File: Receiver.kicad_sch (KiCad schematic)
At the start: 45 parts, among them J2 UFL, J3 UFL, SW2 TS2306A, U1 ESP32-C3, U11 TPRT9013-33, U12 0479480001, U9 SX1280IMLTRT, Y1 40MHz, Y2 52MHz/10ppm

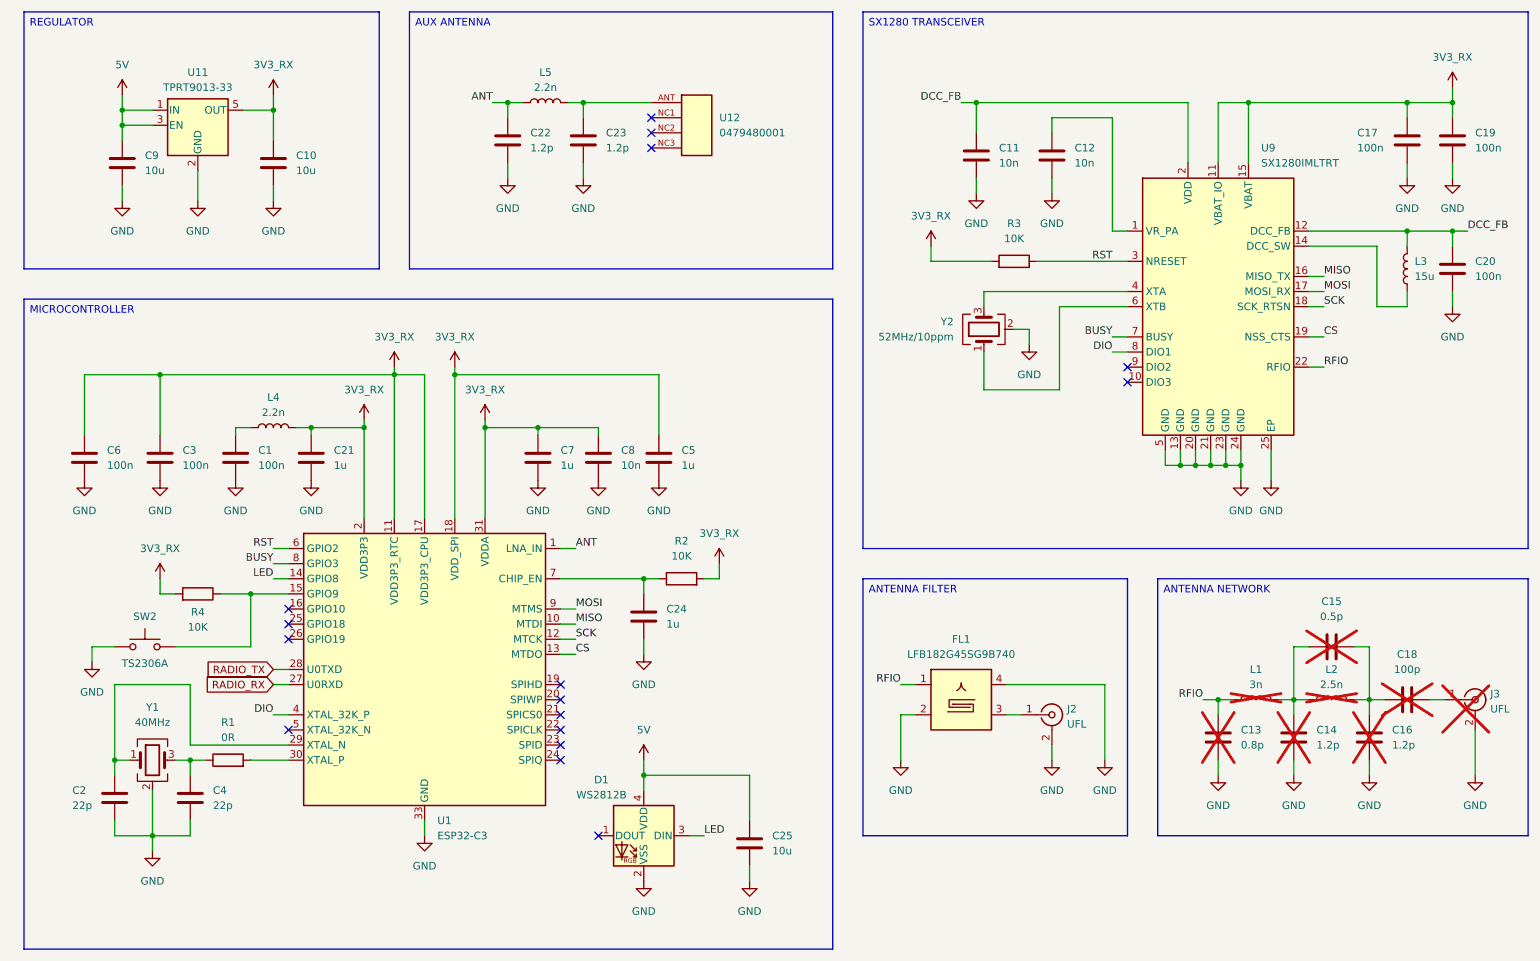
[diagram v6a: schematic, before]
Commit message: Footprints and revision
Added the missing footprints.
Updated a all the schematics.
Completed an initial review of the schematics.

TODO:
Perform a deep review of the schematics before committing to layout.
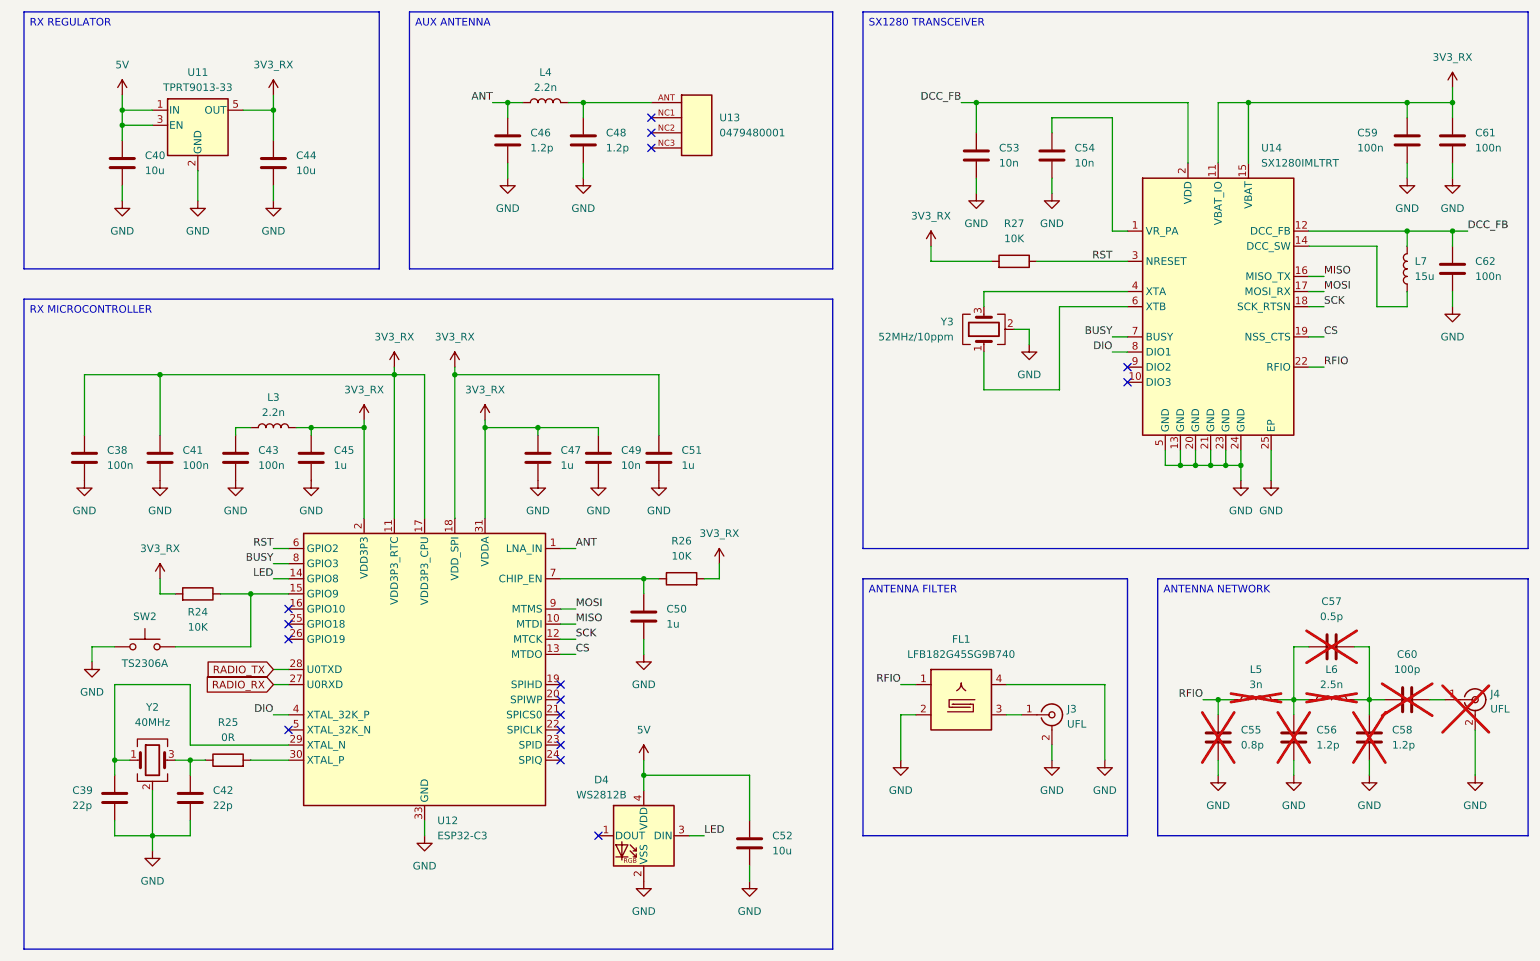
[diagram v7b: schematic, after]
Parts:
- C38: renamed from C6; footprint (none) -> Capacitor_SMD:C_0201_0603Metric
- C39: renamed from C2; footprint (none) -> Capacitor_SMD:C_0201_0603Metric
- C40: renamed from C9; footprint (none) -> Capacitor_SMD:C_0805_2012Metric
- C41: renamed from C3; footprint (none) -> Capacitor_SMD:C_0603_1608Metric
- C42: renamed from C4; footprint (none) -> Capacitor_SMD:C_0603_1608Metric
- C43: renamed from C1; footprint (none) -> Capacitor_SMD:C_0603_1608Metric
- C44: renamed from C10; footprint (none) -> Capacitor_SMD:C_0805_2012Metric
- C45: renamed from C21; footprint (none) -> Capacitor_SMD:C_0603_1608Metric
- C46: renamed from C22; footprint (none) -> Capacitor_SMD:C_0603_1608Metric
- C47: renamed from C7; footprint (none) -> Capacitor_SMD:C_0603_1608Metric
- C48: renamed from C23; footprint (none) -> Capacitor_SMD:C_0603_1608Metric
- C49: renamed from C8; footprint (none) -> Capacitor_SMD:C_0603_1608Metric
- C50: renamed from C24; footprint (none) -> Capacitor_SMD:C_0603_1608Metric
- C51: renamed from C5; footprint (none) -> Capacitor_SMD:C_0603_1608Metric
- C52: renamed from C25; footprint (none) -> Capacitor_SMD:C_0805_2012Metric
- C53: renamed from C11; footprint (none) -> Capacitor_SMD:C_0603_1608Metric
- C54: renamed from C12; footprint (none) -> Capacitor_SMD:C_0603_1608Metric
- C59: renamed from C17; footprint (none) -> Capacitor_SMD:C_0603_1608Metric
- C61: renamed from C19; footprint (none) -> Capacitor_SMD:C_0603_1608Metric
- C62: renamed from C20; footprint (none) -> Capacitor_SMD:C_0603_1608Metric
- L3: renamed from L4; footprint (none) -> Inductor_SMD:L_0603_1608Metric
- L4: renamed from L5; footprint (none) -> Inductor_SMD:L_0603_1608Metric
- L7: renamed from L3; footprint (none) -> Inductor_SMD:L_0603_1608Metric
- R24: renamed from R4; footprint (none) -> Resistor_SMD:R_0603_1608Metric
- R25: renamed from R1; footprint (none) -> Resistor_SMD:R_0603_1608Metric
- R26: renamed from R2; footprint (none) -> Resistor_SMD:R_0603_1608Metric
- R27: renamed from R3; footprint (none) -> Resistor_SMD:R_0603_1608Metric
- renumbered C13 to C55, C14 to C56, C15 to C57, C16 to C58, C18 to C60, D1 to D4, J2 to J3, J3 to J4, L1 to L5, L2 to L6, U1 to U12, U12 to U13, U9 to U14, Y1 to Y2, Y2 to Y3
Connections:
- net GND: no longer FL1.5

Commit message: Receiver and sensors
Updated the receiver schematic.
Updated the sensors schematic.
Removed the ESP32 C3.
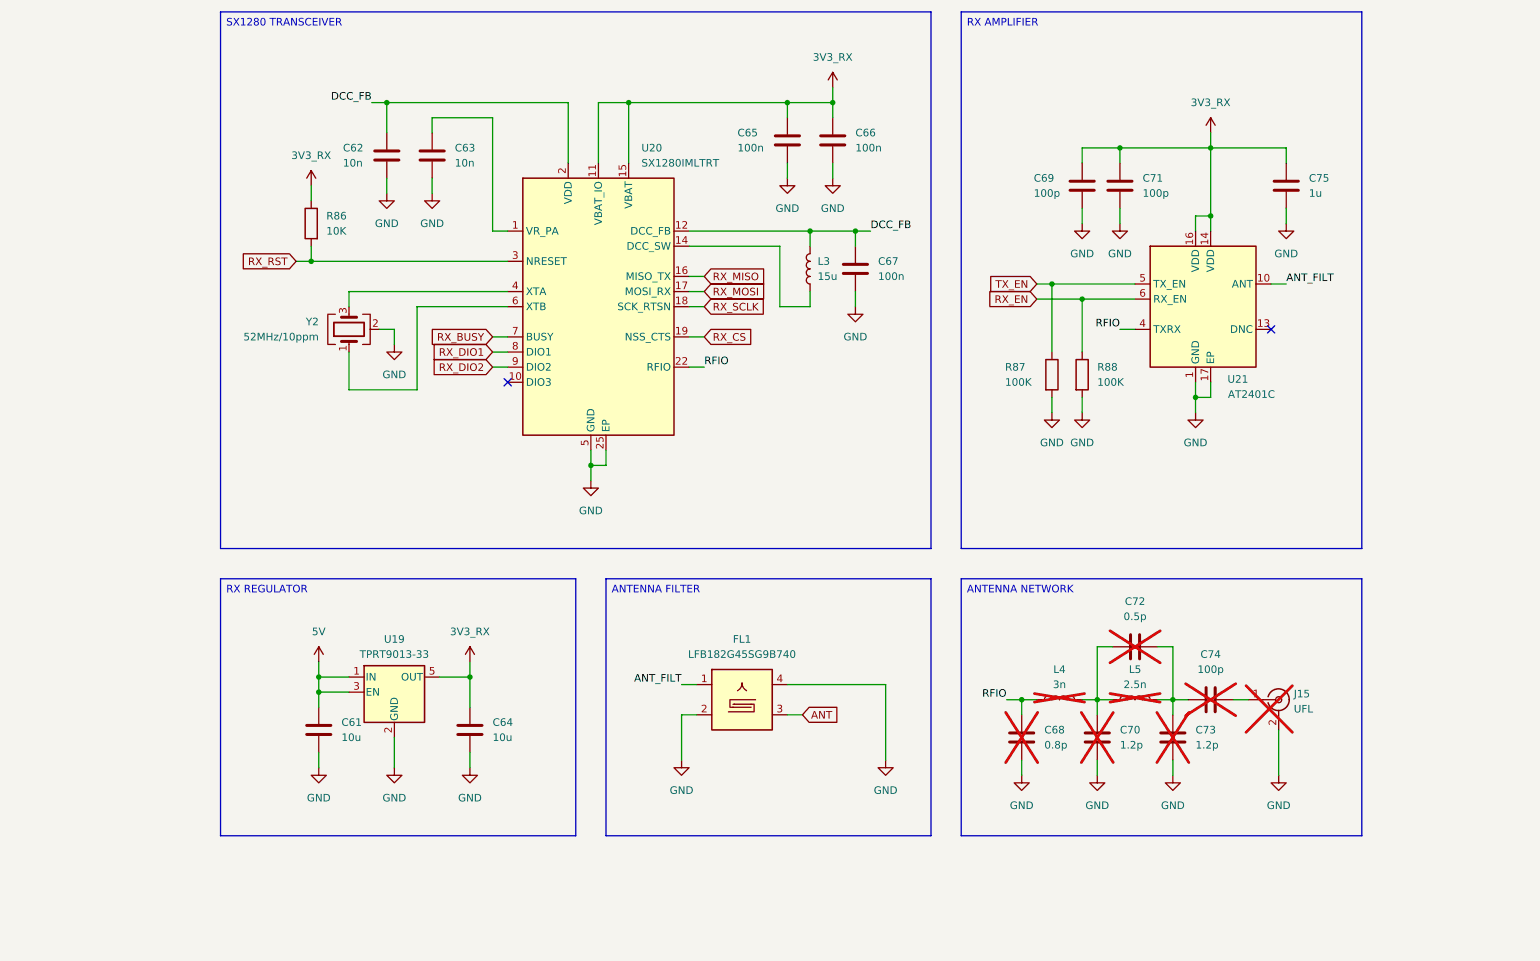
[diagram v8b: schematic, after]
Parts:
- removed C38: 100n, Capacitor_SMD:C_0201_0603Metric, symbol Device:C
- removed C39: 22p, Capacitor_SMD:C_0201_0603Metric, symbol Device:C
- removed C41, C43: 100n, Capacitor_SMD:C_0603_1608Metric, symbol Device:C
- removed C42: 22p, Capacitor_SMD:C_0603_1608Metric, symbol Device:C
- removed C45, C47, C50, C51: 1u, Capacitor_SMD:C_0603_1608Metric, symbol Device:C
- removed C46, C48: 1.2p, Capacitor_SMD:C_0603_1608Metric, symbol Device:C
- removed C49: 10n, Capacitor_SMD:C_0603_1608Metric, symbol Device:C
- removed C52: 10u, Capacitor_SMD:C_0805_2012Metric, symbol Device:C
- removed D4: WS2812B, Custom_Parts:WS2812B-2020, symbol LED:WS2812B-2020
- removed J3: UFL, Connector_Coaxial:U.FL_Hirose_U.FL-R-SMT-1_Vertical, symbol Connector:Conn_Coaxial
- removed L3, L4: 2.2n, Inductor_SMD:L_0603_1608Metric, symbol Device:L
- removed R24, R26: 10K, Resistor_SMD:R_0603_1608Metric, symbol Device:R
- removed R25: 0R, Resistor_SMD:R_0603_1608Metric, symbol Device:R
- removed SW2: TS2306A, Custom_Parts:SW_SMD_3.0x2.0_PUSH, symbol Switch:SW_Push
- removed U12: ESP32-C3, Package_DFN_QFN:QFN-32-1EP_5x5mm_P0.5mm_EP3.7x3.7mm, symbol Custom_Parts:ESP32-C3
- removed U13: 0479480001, Custom_Parts:0479480001, symbol Custom_Parts:0479480001
- removed Y2: 40MHz, Crystal:Crystal_SMD_2016-4Pin_2.0x1.6mm, symbol Device:Crystal_GND24
- added C69, C71: 100p, Capacitor_SMD:C_0603_1608Metric, symbol Device:C
- added C75: 1u, Capacitor_SMD:C_0603_1608Metric, symbol Device:C
- added R87, R88: 100K, Resistor_SMD:R_0603_1608Metric, symbol Device:R
- added U21: AT2401C, Package_DFN_QFN:QFN-16-1EP_3x3mm_P0.5mm_EP1.7x1.7mm_ThermalVias, symbol Custom_Parts:AT2401C
- renumbered C40 to C61, C53 to C62, C54 to C63, C44 to C64, C59 to C65, C61 to C66, C62 to C67, C55 to C68, C56 to C70, C57 to C72, C58 to C73, C60 to C74, J4 to J15, L7 to L3, L5 to L4, L6 to L5, R27 to R86, U11 to U19, U14 to U20, Y3 to Y2
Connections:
- net 3V3_RX: now also R86.1, C69.1, C71.1, C75.1, U21.14 (VDD), U21.16 (VDD); no longer R86.2
- net ANT: now also FL1.3
- net GND: now also C69.2, C71.2, C75.2, R87.2, R88.2, U21.1 (GND), U21.11 (GND), U21.12 (GND), U21.15 (GND), U21.17 (EP), U21.2 (GND), U21.3 (GND), U21.7 (GND), U21.8 (GND), U21.9 (GND)
- net RFIO: now also U21.4 (TXRX); no longer FL1.1
- net RX_DIO2: now reaches U20.9 (DIO2)
- net BUSY renamed RX_BUSY
- net CS renamed RX_CS
- net DIO renamed RX_DIO1
- net MISO renamed RX_MISO
- net MOSI renamed RX_MOSI
- net RST renamed RX_RST
- net RX_RST: now also R86.2; no longer R86.1
- net SCK renamed RX_SCLK
- new net ANT_FILT: FL1.1, U21.10 (ANT)
- new net RX_EN: R88.1, U21.6 (RX_EN)
- new net TX_EN: R87.1, U21.5 (TX_EN)
- no-connect marks 16 -> 2
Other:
- company: (none) -> DavidMolTor
- title: (none) -> THUNDER HORSE
- moved on the sheet: C61, C62, C63, C64, C65, C66, C67, C68, C70, C72, C73, C74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
